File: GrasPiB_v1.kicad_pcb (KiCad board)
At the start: 2 copper layers, 85 x 56 mm, 45 parts, among them J1 DB9_Male, J2 Conn_GPIB, J3 JST_PH, J4 JST_PH, J5 3,5mm Pitch, J6 10pin IDC, U1 RPi_GPIO, U2 MAX3232, U3 SN75160BDW, U4 SN75161BDW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

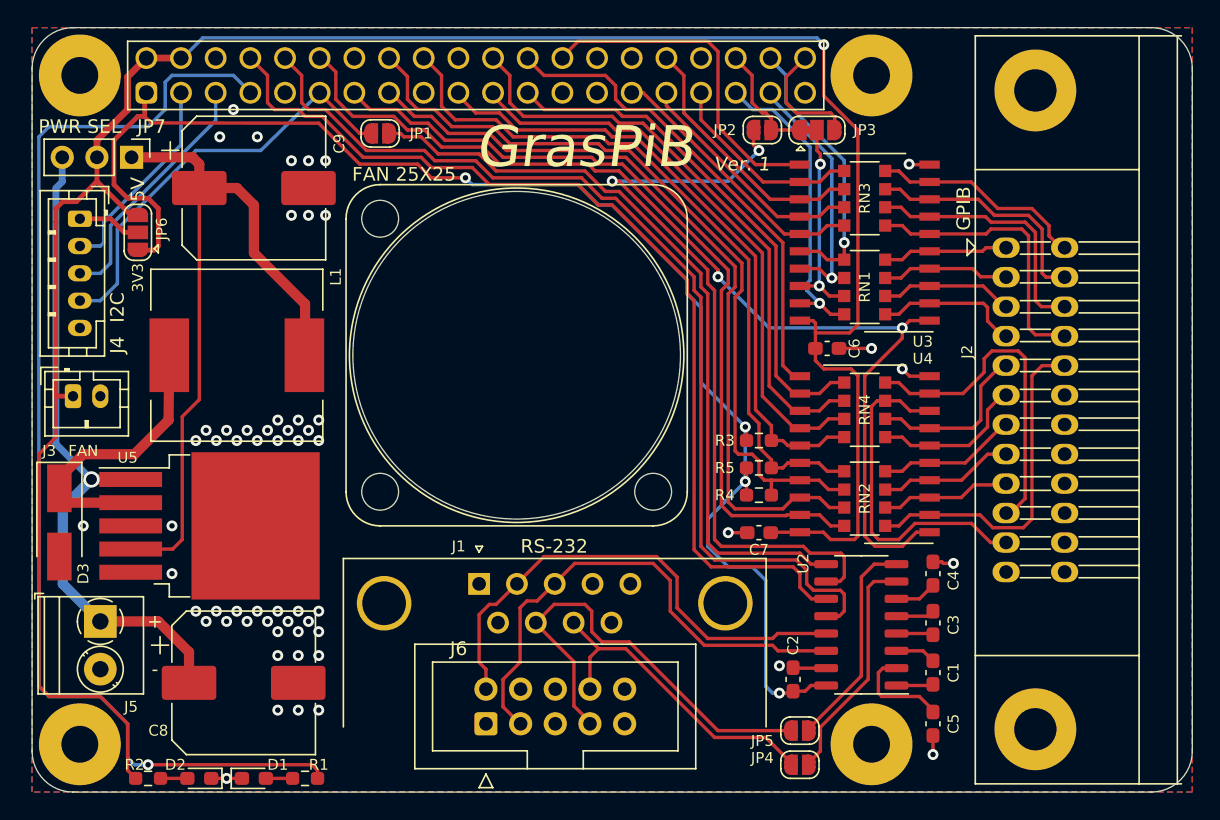
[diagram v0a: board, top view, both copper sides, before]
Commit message: Rewire RTS and CTS signals the correct way
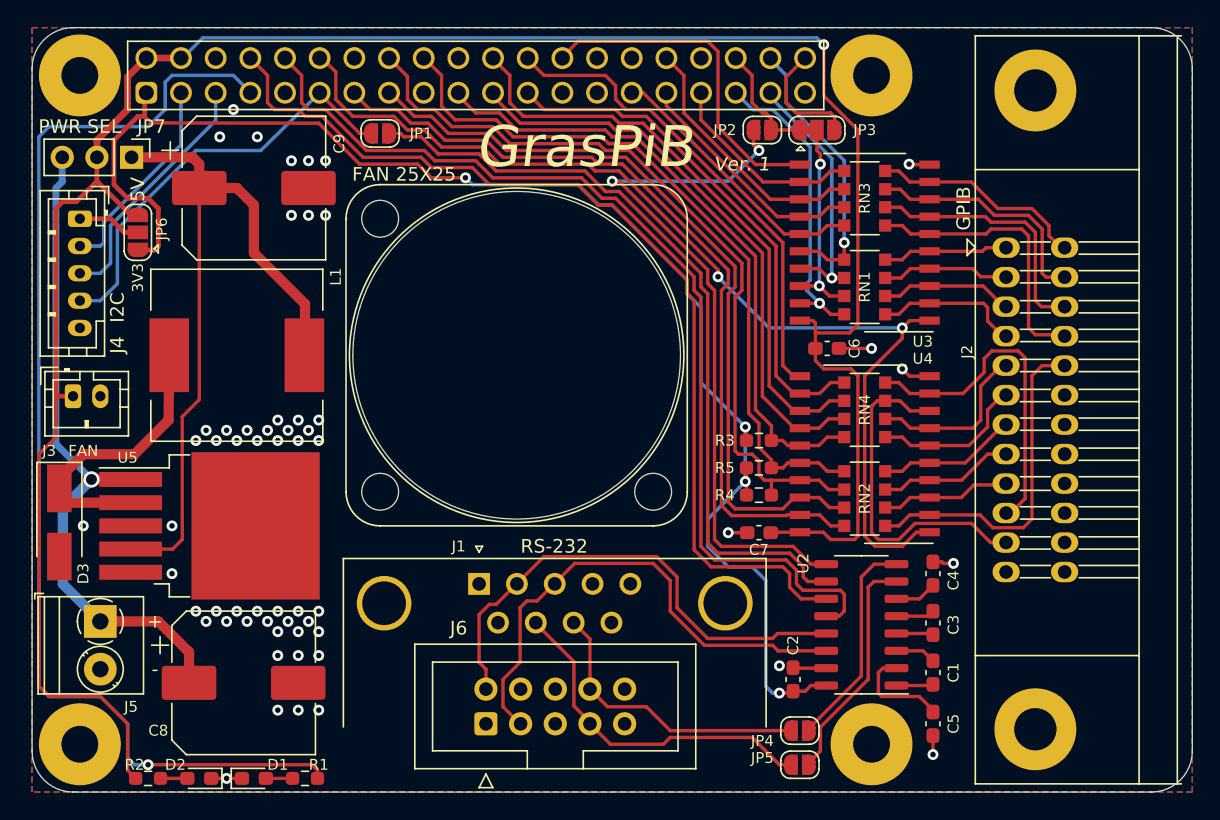
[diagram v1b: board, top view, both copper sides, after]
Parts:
- moved JP4 2.50 mm to (164.8, 105.0)
- moved JP5 2.50 mm to (164.8, 107.5)
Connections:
- U2 pad 10: UART_CTS -> UART_RTS
- U2 pad 7: Net-(JP4-Pad1) -> Net-(JP5-Pad1)
- U2 pad 8: Net-(JP5-Pad1) -> Net-(JP4-Pad1)
- U2 pad 9: UART_RTS -> UART_CTS
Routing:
- net /RS232_RTS: track 33.0 -> 25.4 mm
- net UART_CTS: track 56.0 -> 51.9 mm
- net /RS232_CTS: track 23.6 -> 21.4 mm
- net Net-(JP5-Pad1): track 15.8 -> 17.1 mm
- net Net-(JP4-Pad1): track 17.1 -> 15.8 mm
- net UART_RTS: track 56.4 -> 57.3 mm
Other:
- board text added: "https://github.com/an-ven/graspib"
